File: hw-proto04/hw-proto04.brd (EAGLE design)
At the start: 54.3 x 58.4 mm, 34 parts, among them IC2 UCC27523DR, IC3 MCP2562T, IC4 STM32F042C6T7, IC5 TLV74333PDBVR, J1 10, J2 10, Q1 SQJ147ELP-T1_GE3, Q2 SQJ147ELP-T1_GE3

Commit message: layout refinement
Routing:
- net GND: vias 34 -> 38
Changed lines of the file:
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@@
 <via x="50.4825" y="16.1925" extent="1-16" drill="0.381"/>
 <contactref element="RBOOT0" pad="1"/>
+<via x="26.3525" y="13.0175" extent="1-16" drill="0.381"/>
+<via x="30.1625" y="9.2075" extent="1-16" drill="0.381"/>
+<via x="28.575" y="13.6525" extent="1-16" drill="0.381"/>
+<via x="45.72" y="19.05" extent="1-16" drill="0.381"/>
 </signal>
 <signal name="SW1">
@@
 <contactref element="R1" pad="1"/>
 <contactref element="IC4" pad="34"/>
-<wire x1="23.288" y1="15.72" x2="29.055" y2="15.72" width="0.254" layer="1"/>
 <wire x1="41.275" y1="21.59" x2="34.925" y2="21.59" width="0.254" layer="1"/>
-<wire x1="34.925" y1="21.59" x2="29.055" y2="15.72" width="0.254" layer="1"/>
+<wire x1="34.925" y1="21.59" x2="29.5275" y2="16.1925" width="0.254" layer="1"/>
+<wire x1="23.288" y1="15.72" x2="24.61" y2="15.72" width="0.254" layer="1"/>
+<wire x1="24.61" y1="15.72" x2="25.0825" y2="16.1925" width="0.254" layer="1"/>
+<wire x1="25.0825" y1="16.1925" x2="29.5275" y2="16.1925" width="0.254" layer="1"/>
 </signal>
 <signal name="N$3">

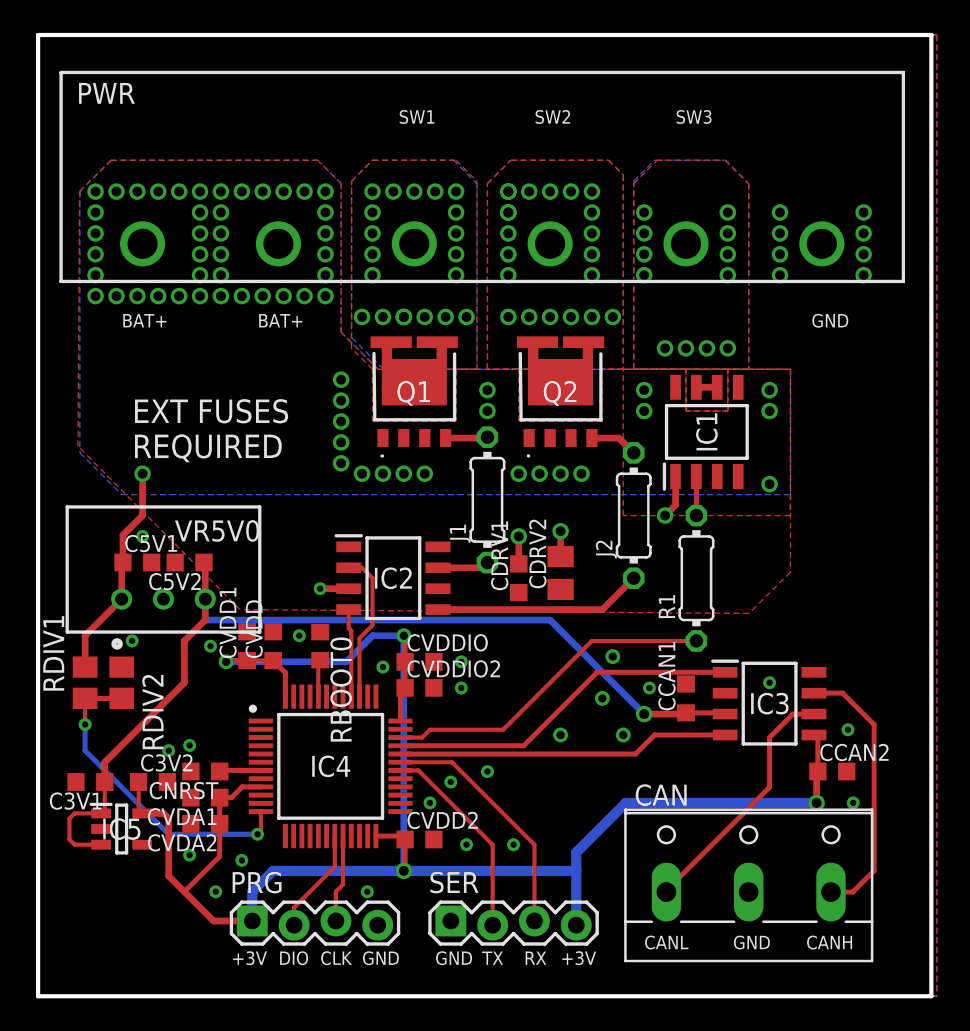
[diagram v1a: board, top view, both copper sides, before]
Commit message: added term resistor, layout refinement
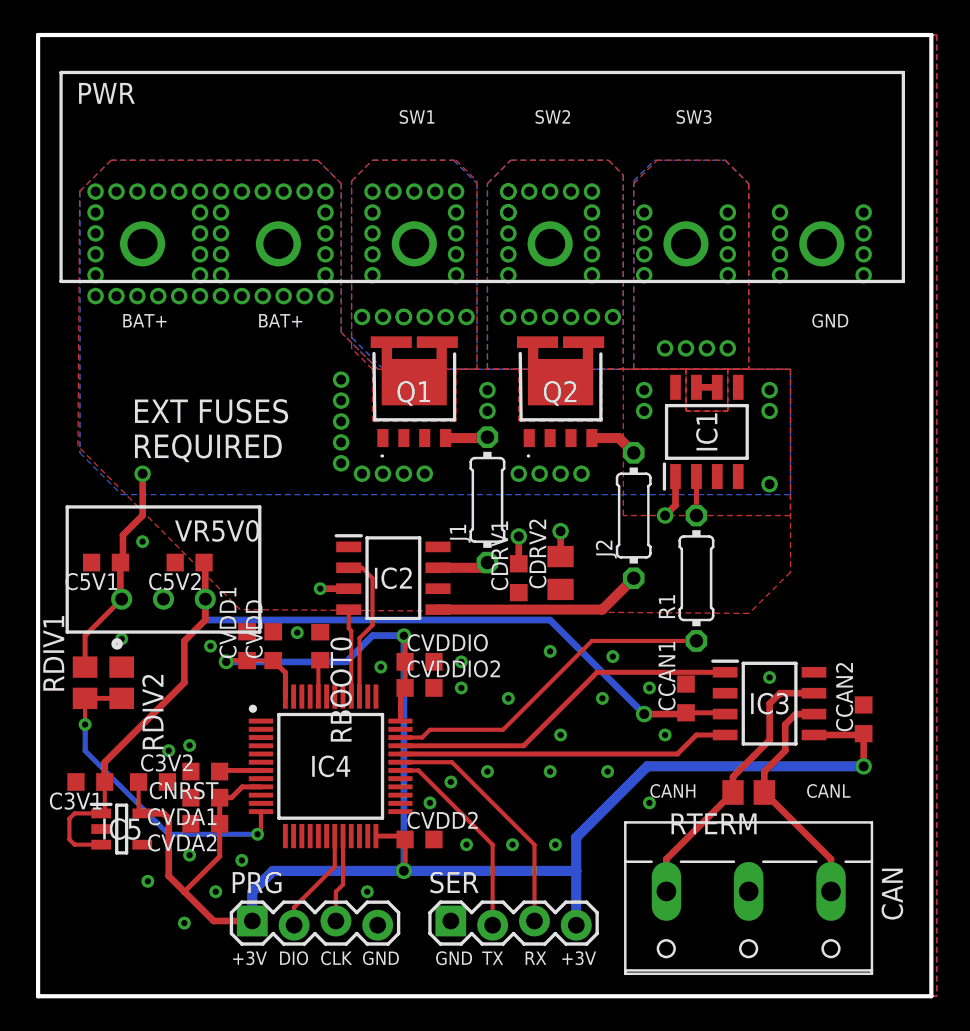
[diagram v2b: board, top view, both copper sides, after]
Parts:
- added RTERM: 120R, rcl:R0805
- moved CCAN2 3.70 mm to (51.4, 16.8), turned to 90 degrees
- moved CAN 2.54 mm to (44.5, 5.08), turned to 180 degrees
- moved C5V1 1.91 mm to (5.40, 26.4), turned to 180 degrees
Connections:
- net CANH: now also RTERM.2
- net CANL: now also RTERM.1
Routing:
- net +3V3: track 109.7 -> 114.8 mm
- net CANL: track 15.3 -> 14.4 mm
- net GND: vias 38 -> 44

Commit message: schematic refinements
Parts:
- removed J2: 10, rcl:0204/7
- added R2: 10, rcl:0204/7
- IC4: value STM32F042C6T7 -> STM32F042
- IC5: value TLV74333PDBVR -> TLV74333P
- Q1, Q2: value SQJ147ELP-T1_GE3 -> (none)
- renumbered J1 to R3, PRG to SWLINK, SER to UART1
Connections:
- net +3V3: now also UART1.1; no longer UART1.4
- net GND: now also SWLINK.2, UART1.2; no longer SWLINK.4, UART1.1
- net N$3: now also R2.1; no longer J2.1
- net N$6: now also R2.2; no longer J2.2
- net RX1: now also UART1.4; no longer UART1.3
- net SWCLK: now also SWLINK.4; no longer SWLINK.3
- net SWDIO: now also SWLINK.3; no longer SWLINK.2
- net TX1: now also UART1.3; no longer UART1.2
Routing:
- net +3V3: track 114.8 -> 113.3 mm
- net RX1: track 14.9 -> 16.2 mm
- net SWDIO: track 6.44 -> 5.19 mm
- net N$3: track 12.7 -> 13.6 mm
- net SWCLK: track 5.34 -> 6.29 mm
- net TX1: track 12.4 -> 13.2 mm
- net GND: vias 44 -> 45
- net +12V: vias 61 -> 63
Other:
- board text added: "EXTERNAL FUSING REQUIRED"
- board text removed: "EXT FUSES REQUIRED"

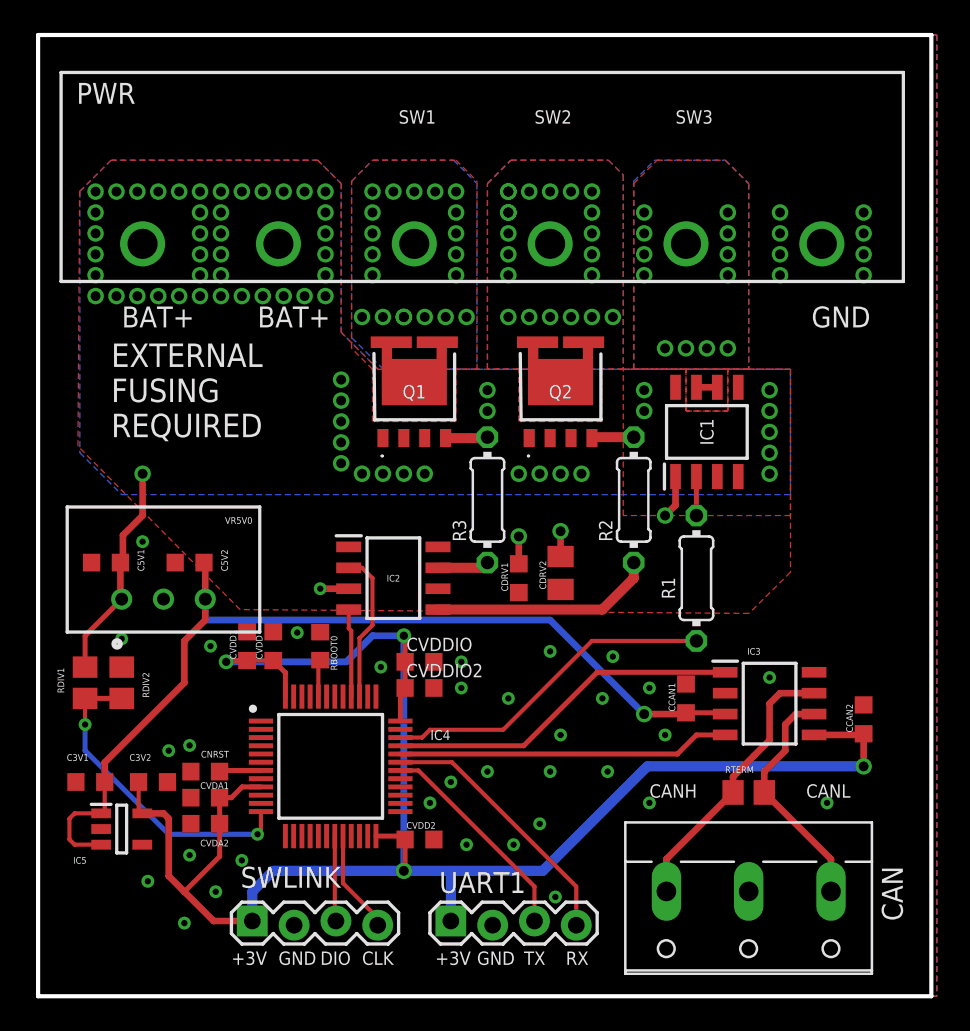
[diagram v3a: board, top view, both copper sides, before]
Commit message: silkscreen refinement
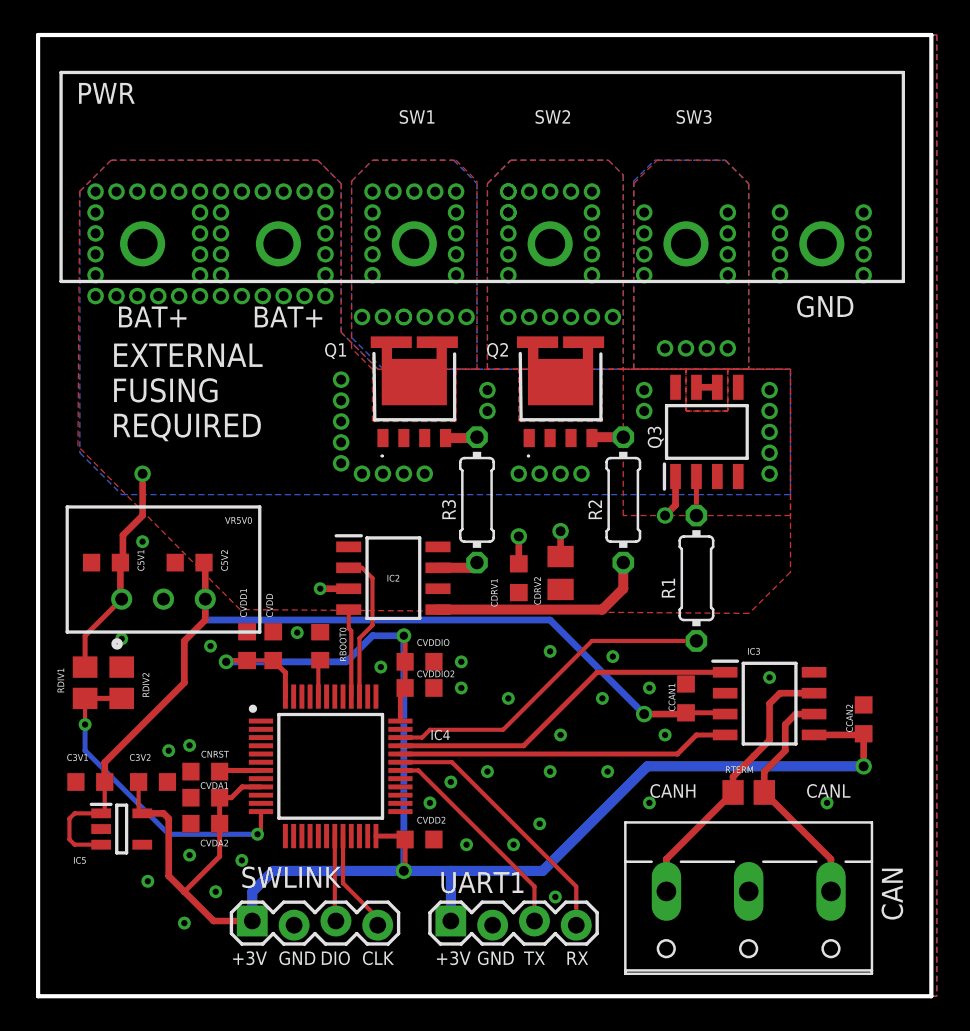
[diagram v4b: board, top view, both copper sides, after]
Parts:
- CVDDIO: value 100n -> 4u7
- CVDDIO2: value 4u7 -> 100n
- moved R2 0.64 mm to (36.8, 30.2)
- moved R3 0.63 mm to (27.9, 30.2)
- renumbered IC1 to Q3
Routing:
- net N$6: track 2.56 -> 1.93 mm
- net N$5: track 2.56 -> 1.93 mm
- net N$4: track 3.13 -> 2.50 mm

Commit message: Updated documentation for hw-proto04
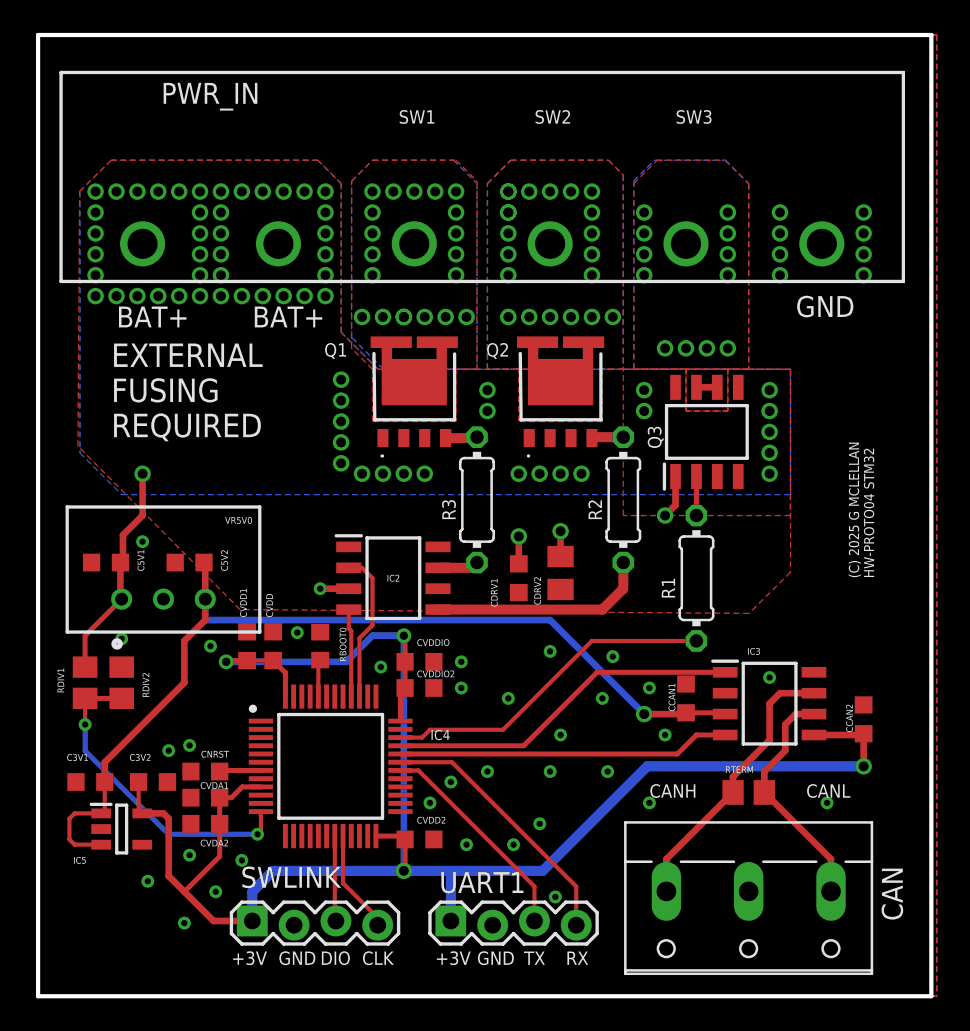
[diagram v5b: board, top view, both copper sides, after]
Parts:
- IC2: value UCC27523DR -> FET DRIVER
- Q1, Q2: value (none) -> FET SW
- Q3: value (none) -> SMART FET
- renumbered PWR to PWR_IN
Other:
- board text added: "(C) 2025 G MCLELLAN HW-PROTO04 STM32"
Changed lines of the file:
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@@
 <text x="40.005" y="53.0225" size="0.8128" layer="25" font="vector" ratio="12">SW3</text>
 <text x="47.3075" y="41.275" size="1.27" layer="25" font="vector" ratio="14">GND</text>
+<text x="52.07" y="25.4" size="0.6096" layer="25" ratio="14" rot="R90">(C) 2025 G MCLELLAN
+HW-PROTO04 STM32</text>
 </plain>
 <attributes>
@@
 </autorouter>
 <elements>
-<element name="Q3" library="VN5E160MSTR-E" package="SOIC127P600X175-8N" value="" x="41.91" y="34.29" smashed="yes" rot="R90">
+<element name="Q3" library="VN5E160MSTR-E" package="SOIC127P600X175-8N" value="SMART FET" x="41.91" y="34.29" smashed="yes" rot="R90">
 <attribute name="MANUFACTURER_PART_NUMBER" value="VN5E160MSTR-E" x="41.91" y="34.29" size="1.778" layer="27" rot="R90" display="off"/>
 <attribute name="DESCRIPTION" value="Gate Drivers SNGL CH HI-SIDE DRVR W/ANALOG CRRNT SNSE" x="41.91" y="34.29" size="1.778" layer="27" rot="R90" display="off"/>
@@
 <attribute name="MOUSER_PRICE-STOCK" value="https://www.mouser.co.uk/ProductDetail/STMicroelectronics/VN5E160MSTR-E?qs=WSSg0AwdCh77XxtxsYEeyw%3D%3D" x="41.91" y="34.29" size="1.778" layer="27" rot="R90" display="off"/>
 <attribute name="NAME" x="38.735" y="33.9725" size="0.8128" layer="25" font="vector" ratio="14" rot="R90" align="center"/>
-<attribute name="VALUE" x="41.91" y="34.29" size="1.27" layer="27" rot="R90" align="center"/>
+<attribute name="VALUE" x="42.545" y="33.02" size="0.4064" layer="27" ratio="14" align="center"/>
 </element>
 <element name="IC3" library="MCP2562T-H_SN" package="SOIC127P600X175-8N" value="MCP2562T" x="45.72" y="17.78" smashed="yes">
@@
 <attribute name="VALUE" x="47.9425" y="20.955" size="0.4064" layer="27" font="vector" ratio="14" align="center"/>
 </element>
-<element name="PWR" library="4DB-P108-06" package="4DBP10806" value="" x="7.62" y="45.72" smashed="yes">
+<element name="PWR_IN" library="4DB-P108-06" package="4DBP10806" value="" x="7.62" y="45.72" smashed="yes">
 <attribute name="MANUFACTURER_PART_NUMBER" value="4DB-P108-06" x="7.62" y="45.72" size="1.778" layer="27" display="off"/>
 <attribute name="DESCRIPTION" value="Dual Barrier, Printed Circuit Pin, Wire-to-Board, 6 Position, 8.26 mm [.325 in] Centerline, 1 Row, Buchanan 4DB Series, Barrier Strips" x="7.62" y="45.72" size="1.778" layer="27" display="off"/>
@@
 <attribute name="HEIGHT" value="13.716mm" x="7.62" y="45.72" size="1.778" layer="27" display="off"/>
 <attribute name="MOUSER_PRICE-STOCK" value="https://www.mouser.co.uk/ProductDetail/TE-Connectivity/4DB-P108-06?qs=JZD3Rbs9Xzm1xbyNfnCHaQ%3D%3D" x="7.62" y="45.72" size="1.778" layer="27" display="off"/>
-<attribute name="NAME" x="5.398" y="54.864" size="1.27" layer="25" align="center"/>
+<attribute name="NAME" x="11.748" y="54.864" size="1.27" layer="25" align="center"/>
 <attribute name="VALUE" x="28.258" y="49.784" size="1.27" layer="27" align="center"/>
 </element>
@@
 <attribute name="VALUE" x="52.235" y="19.43" size="0.4064" layer="27" font="vector" ratio="14" rot="R180"/>
 </element>
-<element name="Q1" library="transistor-vishay-pchan-pso8" package="SQJ147ELPT1_GE3" value="" x="24.13" y="36.83" smashed="yes">
+<element name="Q1" library="transistor-vishay-pchan-pso8" package="SQJ147ELPT1_GE3" value="FET SW" x="24.13" y="36.83" smashed="yes">
 <attribute name="DESCRIPTION" value="MOSFET P-CHANNEL 40-V (D-S) 175C MOSFET" x="24.13" y="36.83" size="1.778" layer="27" display="off"/>
 <attribute name="MANUFACTURER_NAME" value="Vishay" x="24.13" y="36.83" size="1.778" layer="27" display="off"/>
@@
 <attribute name="VALUE" x="24.13" y="36.733" size="0.8128" layer="27" font="vector" ratio="14" align="center"/>
 </element>
-<element name="Q2" library="transistor-vishay-pchan-pso8" package="SQJ147ELPT1_GE3" value="" x="33.02" y="36.83" smashed="yes">
+<element name="Q2" library="transistor-vishay-pchan-pso8" package="SQJ147ELPT1_GE3" value="FET SW" x="33.02" y="36.83" smashed="yes">
 <attribute name="DESCRIPTION" value="MOSFET P-CHANNEL 40-V (D-S) 175C MOSFET" x="33.02" y="36.83" size="1.778" layer="27" display="off"/>
 <attribute name="MANUFACTURER_NAME" value="Vishay" x="33.02" y="36.83" size="1.778" layer="27" display="off"/>
@@
 <attribute name="VALUE" x="13.2725" y="14.77" size="0.4064" layer="27" font="vector" ratio="14" rot="R270"/>
 </element>
-<element name="IC2" library="UCC27523DR-fet-driver" package="SOIC127P600X175-8N" value="UCC27523DR" x="22.86" y="25.4" smashed="yes">
+<element name="IC2" library="UCC27523DR-fet-driver" package="SOIC127P600X175-8N" value="FET DRIVER" x="22.86" y="25.4" smashed="yes">
 <attribute name="MOUSER_PART_NUMBER" value="595-UCC27523DR" x="22.86" y="25.4" size="1.778" layer="27" display="off"/>
 <attribute name="MANUFACTURER_NAME" value="Texas Instruments" x="22.86" y="25.4" size="1.778" layer="27" display="off"/>
@@
 <contactref element="Q3" pad="7"/>
 <wire x1="42.545" y1="37.002" x2="41.275" y2="37.002" width="0.4064" layer="1"/>
-<contactref element="PWR" pad="5"/>
+<contactref element="PWR_IN" pad="5"/>
 <polygon width="0.4064" layer="1" spacing="0.3048" isolate="0.254" rank="3">
 <vertex x="40.64" y="35.56"/>
@@
 <contactref element="CCAN1" pad="2"/>
 <contactref element="CCAN2" pad="2"/>
-<contactref element="PWR" pad="6"/>
+<contactref element="PWR_IN" pad="6"/>
 <contactref element="CVDD2" pad="2"/>
 <contactref element="IC2" pad="3"/>
@@
 </signal>
 <signal name="SW1">
-<contactref element="PWR" pad="3"/>
+<contactref element="PWR_IN" pad="3"/>
 <polygon width="0.4064" layer="1" spacing="0.3048" isolate="0.254">
 <vertex x="21.59" y="38.1"/>
@@
 <vertex x="30.48" y="38.1"/>
 </polygon>
-<contactref element="PWR" pad="4"/>
+<contactref element="PWR_IN" pad="4"/>
 <polygon width="0.4064" layer="16" spacing="0.3048" isolate="0.254" thermals="no" rank="2">
 <vertex x="28.575" y="38.1"/>
@@
 </signal>
 <signal name="+12V">
-<contactref element="PWR" pad="1"/>
+<contactref element="PWR_IN" pad="1"/>
 <contactref element="VR5V0" pad="1"/>
 <polygon width="0.4064" layer="1" spacing="0.3048" isolate="0.254" rank="4">
@@
 <via x="38.1" y="36.83" extent="1-16" drill="0.6"/>
 <via x="38.1" y="35.56" extent="1-16" drill="0.6"/>
-<contactref element="PWR" pad="2"/>
+<contactref element="PWR_IN" pad="2"/>
 <via x="19.685" y="37.465" extent="1-16" drill="0.6"/>
 <contactref element="IC2" pad="6"/>
